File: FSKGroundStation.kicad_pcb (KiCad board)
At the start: 4 copper layers, 100 x 82 mm, 196 parts, among them J1 FTSH-105-01-L-DV-K, J10 CX90B1-24P, J11 HTSW-102-07-G-S, J2 HTSW-102-07-G-S, J22 BWSMA-KWE-Z001, J23 SJ-3524-SMT, J24 HTSW-103-07-G-S, J3 CX90B1-24P, J4 BWSMA-KWE-Z001, J5 BWSMA-KWE-Z001, J9 HTSW-102-07-G-S, Q1 BSS138, Q2 BSS138, U1 TPSM861253RDXR, U10 74LVC1GU04DRL, U2 CC1312R1F3RGZR, U3 CY7C65215-32LTXI, U4 CC1125RHBR, U5 GRF5604, U6 SKYA21003, U7 GRF5604, U8 TPD4E004DRYR, U9 SKYA21003, Y1 OW7EL89CENUYO3YLC-40M, Y2 OW7EL89CANUXK7YLC-48M

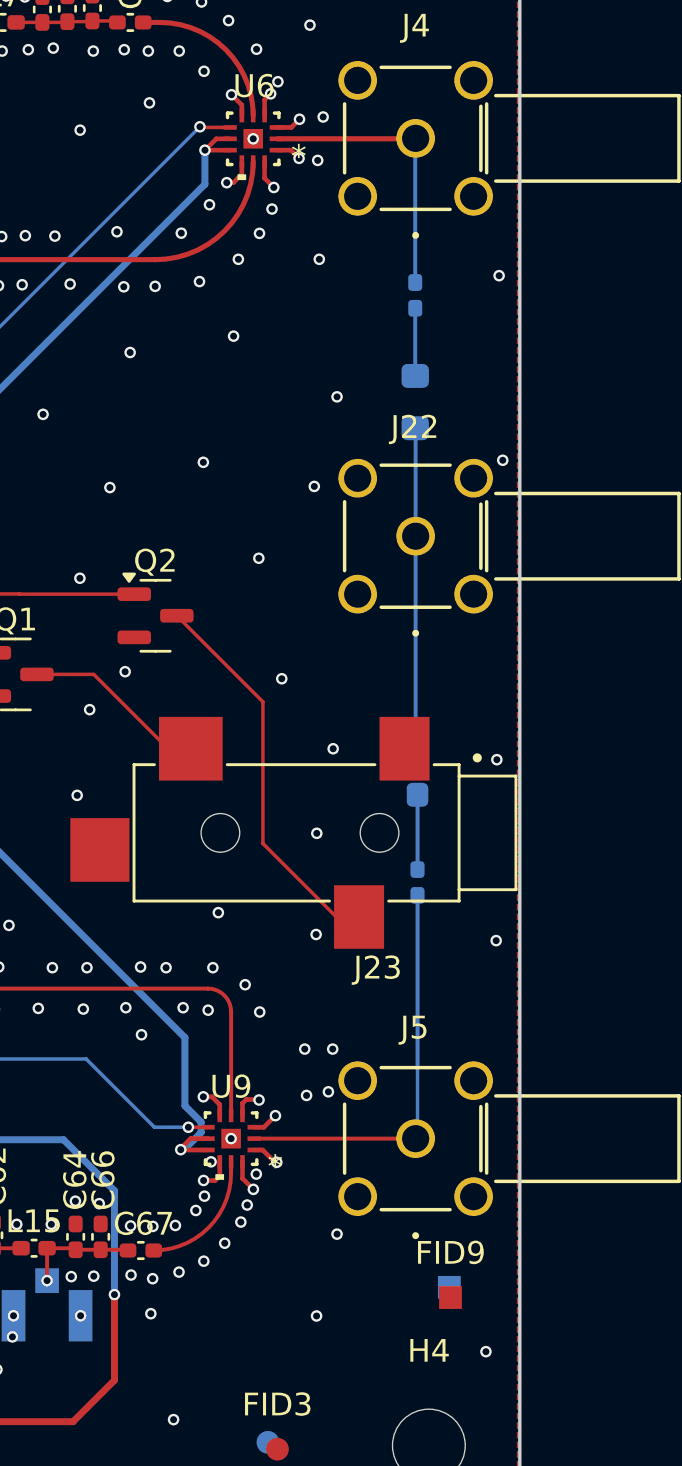
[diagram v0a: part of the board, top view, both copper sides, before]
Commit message: Add bleed-off inductor/resistors to the antenna jacks
Signed-off-by: Corey Minyard <corey@minyard.net>
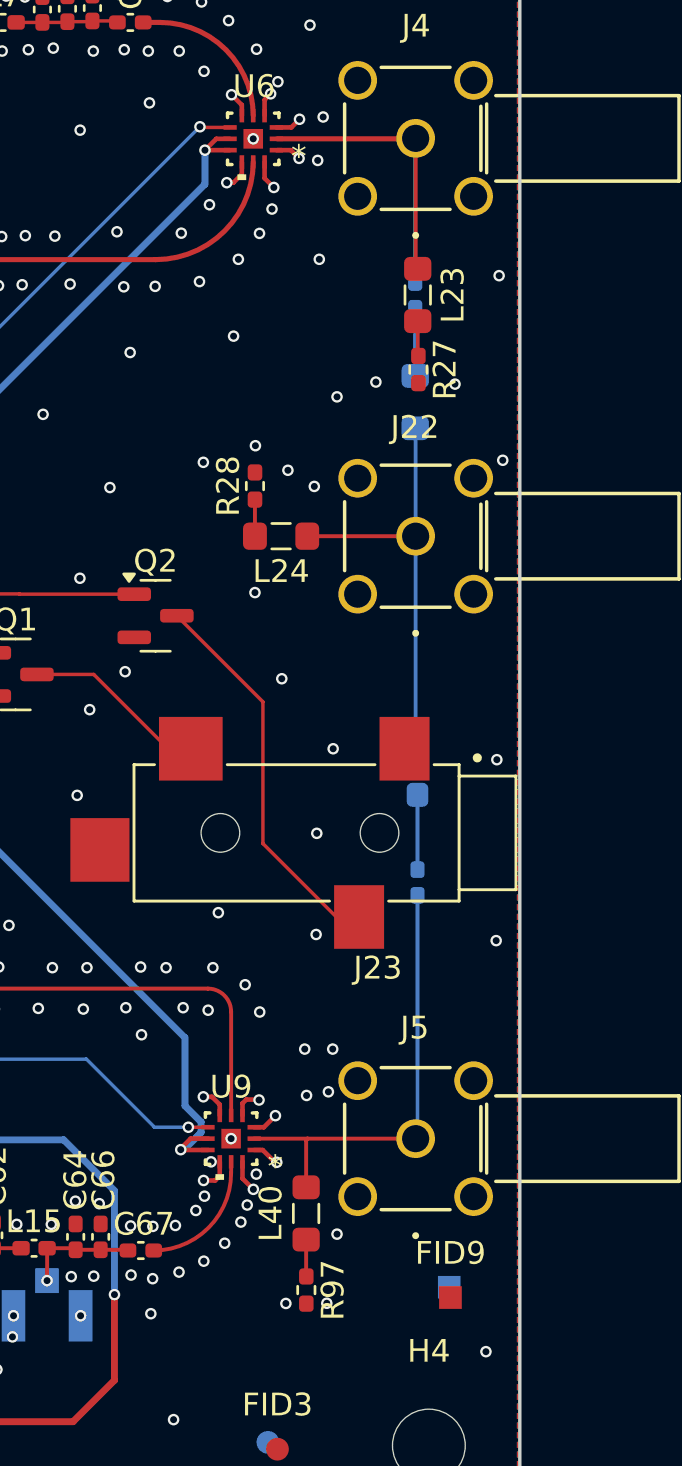
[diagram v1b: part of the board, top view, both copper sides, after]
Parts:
- added L23: 470nH, Inductor_SMD:L_0805_2012Metric_Pad1.05x1.20mm_HandSolder, F.Cu at (165.5, 85.4)
- added L24: 470nH, Inductor_SMD:L_0805_2012Metric_Pad1.05x1.20mm_HandSolder, F.Cu at (159.5, 96.0)
- added L40: 470nH, Inductor_SMD:L_0805_2012Metric_Pad1.05x1.20mm_HandSolder, F.Cu at (160.6, 125.8)
- added R27: 10KΩ, Resistor_SMD:R_0402_1005Metric_Pad0.72x0.64mm_HandSolder, F.Cu at (165.5, 88.7)
- added R28: 10KΩ, Resistor_SMD:R_0402_1005Metric_Pad0.72x0.64mm_HandSolder, F.Cu at (158.3, 93.8)
- added R97: 10KΩ, Resistor_SMD:R_0402_1005Metric_Pad0.72x0.64mm_HandSolder, F.Cu at (160.6, 129.2)
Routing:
- net RF_144: track 12.4 -> 18.2 mm
- net Net-(J22-Pad1): track 14.3 -> 19.0 mm
- net RF_440: track 17.7 -> 19.9 mm
- net Net-(L40-Pad2): track 0.00 -> 1.63 mm
- net Net-(L24-Pad2): track 0.00 -> 1.61 mm
- net Net-(L23-Pad2): track 0.00 -> 1.54 mm
- net GND: vias 605 -> 610

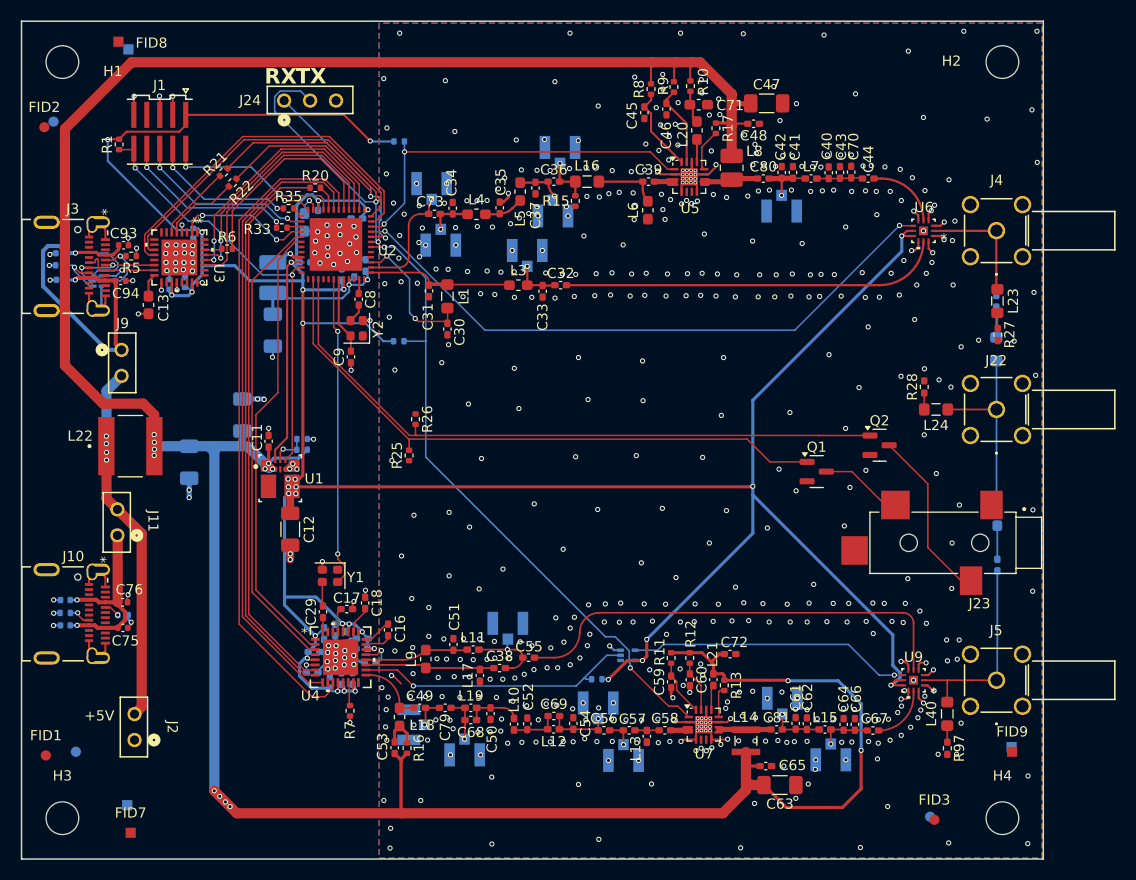
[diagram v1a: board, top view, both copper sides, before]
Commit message: Add a barrel-type power connector
Make supplying power a little simpler.

Signed-off-by: Corey Minyard <corey@minyard.net>
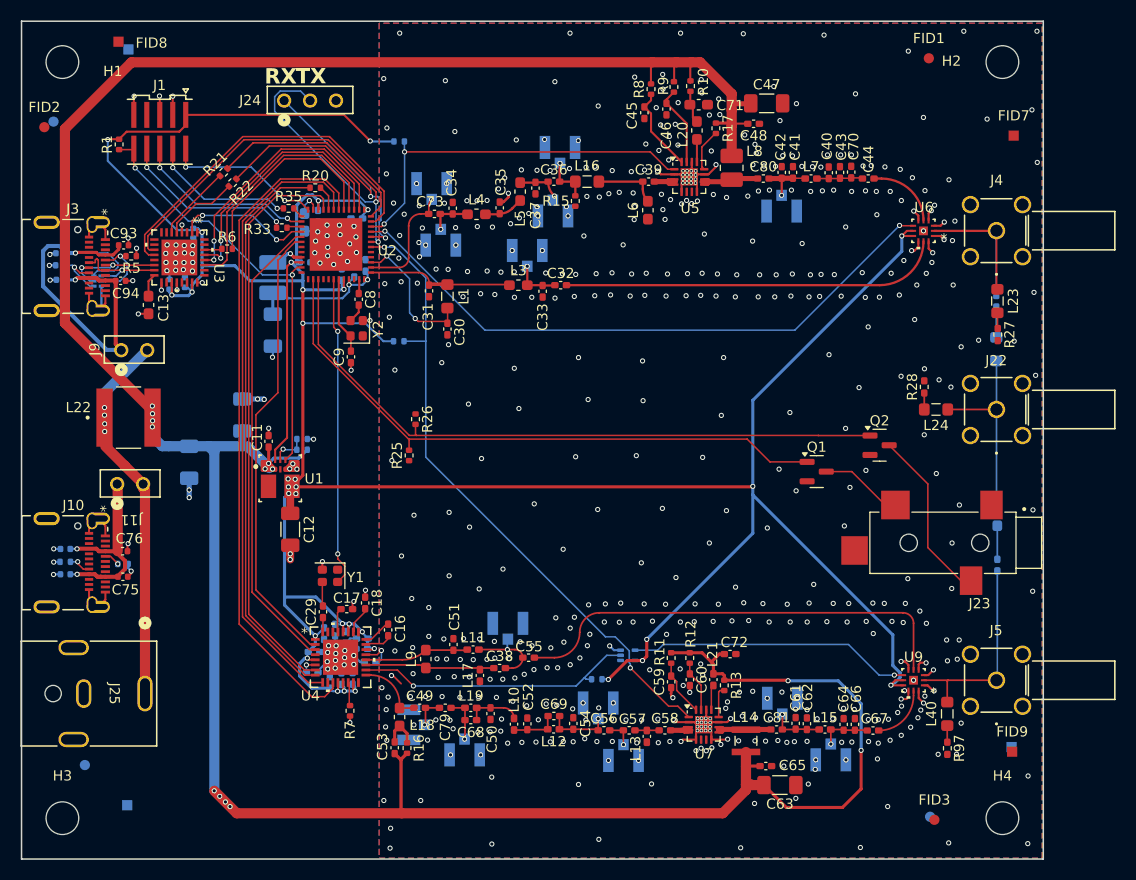
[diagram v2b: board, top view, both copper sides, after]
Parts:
- removed J2: HTSW-102-07-G-S, footprints:CON2_1X2_TU_TSW
- added J25: PJ-063BH, footprints:PJ-063BH_CUD, F.Cu at (82.1, 123.8)
- moved FID1 110.1 mm to (158.8, 61.6)
- moved FID7 110.1 mm to (167.1, 69.2)
- moved C74 5.00 mm to (74.3, 109.7)
- moved C75 5.00 mm to (79.9, 112.4)
- moved C76 5.00 mm to (79.9, 109.9)
- moved C77 5.00 mm to (74.3, 112.1)
- moved J10 5.00 mm to (74.2, 111.0)
- moved R18 5.00 mm to (79.9, 111.1)
- moved R19 5.00 mm to (74.3, 110.9)
- moved J11 3.95 mm to (80.6, 103.3), turned to 0 degrees
- moved L22 2.80 mm to (80.5, 96.8)
- moved J9 1.75 mm to (81.0, 90.2), turned to 0 degrees
- moved FID4 1.57 mm to (76.2, 130.8)
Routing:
- net +5V: track 291.2 -> 288.4 mm
- net Net-(C81-Pad1): track 5.15 -> 6.19 mm
- net +5Vin: track 37.7 -> 38.5 mm
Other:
- board text removed: "+5V"

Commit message: Fix the 440 PA to work at 430-450
Signed-off-by: Corey Minyard <corey@minyard.net>
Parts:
- C66: value 1.8pF 1% -> 5.6pF 1%

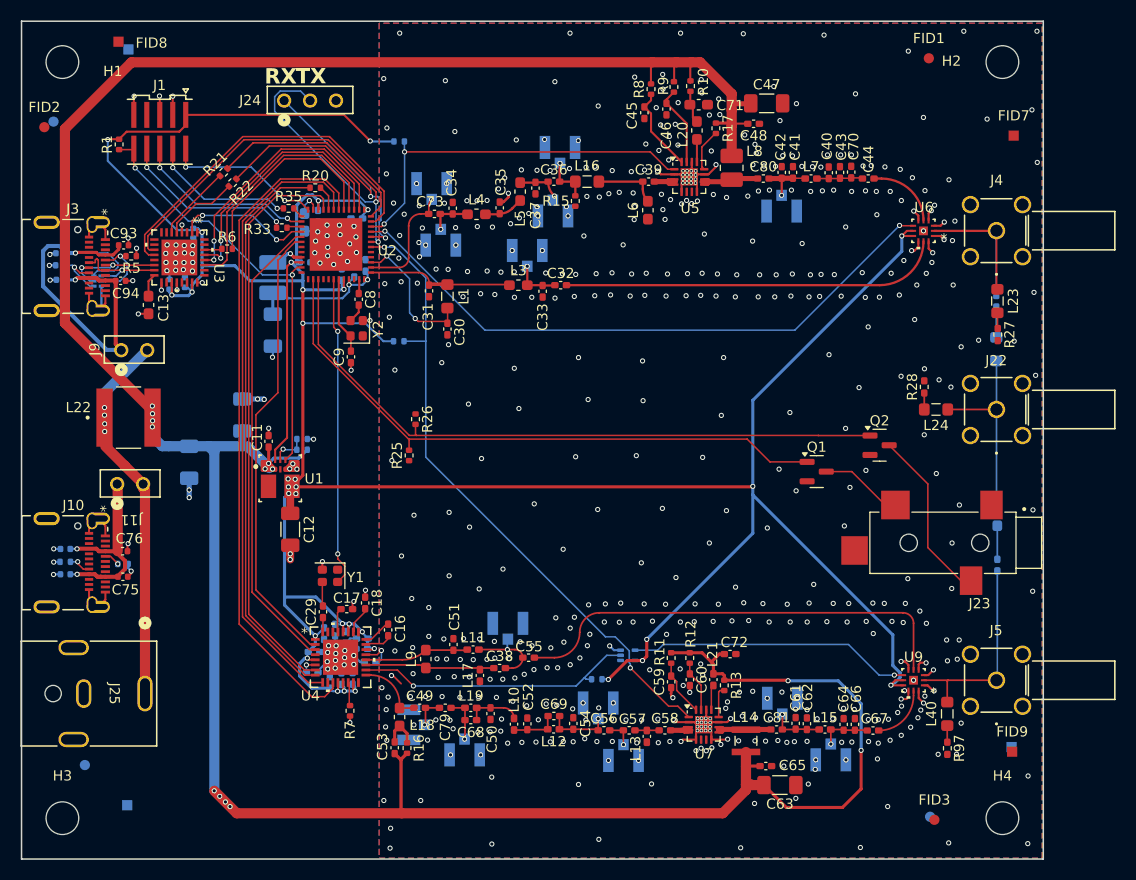
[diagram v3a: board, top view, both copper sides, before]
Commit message: Move RF parts from the bottom of the board to the top
This will allow a heat sink to be more easily mounted.

Signed-off-by: Corey Minyard <corey@minyard.net>
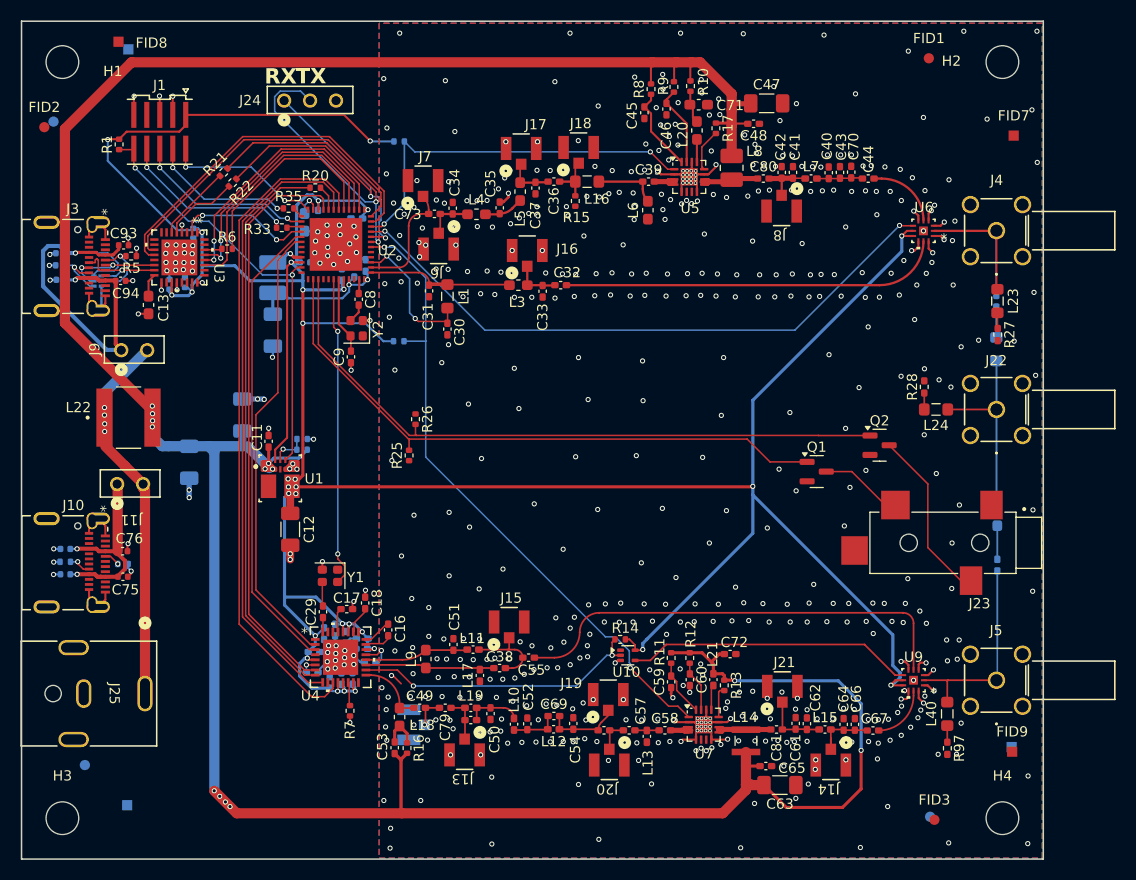
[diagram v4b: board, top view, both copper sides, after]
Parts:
- J13, J14, J15, J16, J17, J18, J19, J20, J21, J6, J7, J8, R14, U10: moved to F.Cu
- moved J17 7.30 mm to (118.9, 70.5)
- moved R14 4.52 mm to (128.6, 118.5)
- moved J18 1.82 mm to (124.5, 70.4), turned to 0 degrees
- moved J20 1.46 mm to (127.5, 130.8), turned to 180 degrees
- moved J19 1.28 mm to (127.4, 123.9), turned to 0 degrees
- moved J21 1.17 mm to (144.5, 123.1), turned to 0 degrees
- moved J7 0.89 mm to (109.3, 73.6), turned to 0 degrees
- moved J14 0.51 mm to (149.2, 130.8), turned to 180 degrees
- moved J6 0.44 mm to (110.8, 80.3), turned to 180 degrees
- moved J15 0.18 mm to (117.7, 116.8), turned to 0 degrees
- turned J13 to 180 degrees
- turned J16 to 0 degrees
- turned J8 to 180 degrees
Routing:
- net +3.3V: track 332.4 -> 328.3 mm, vias 32 -> 30
- net Net-(J21-In): track 5.00 -> 6.20 mm, vias 1 -> 0
- net Net-(J14-In): track 4.88 -> 5.93 mm, vias 1 -> 0
- net 440_TRX_SW: track 27.5 -> 28.5 mm, vias 1 -> 2
- net Net-(J19-In): track 6.08 -> 6.78 mm, vias 1 -> 0
- net GND: track 104.1 -> 103.5 mm, vias 610 -> 609
- net Net-(J20-In): track 2.70 -> 3.20 mm, vias 1 -> 0
- net Net-(U9-CTRL): track 27.7 -> 28.1 mm, vias 1 -> 0
- net Net-(J17-In): track 4.07 -> 4.33 mm, vias 1 -> 0
- net Net-(J6-In): track 3.90 -> 4.13 mm, vias 1 -> 0
- net 144MHz_RF_N: track 11.5 -> 11.8 mm, vias 1 -> 0
- net Net-(J15-In): track 7.93 -> 8.12 mm, vias 1 -> 0
- net Net-(J18-In): track 4.74 -> 4.86 mm, vias 1 -> 0
- net Net-(J8-In): vias 1 -> 0
- net Net-(J16-In): vias 1 -> 0
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
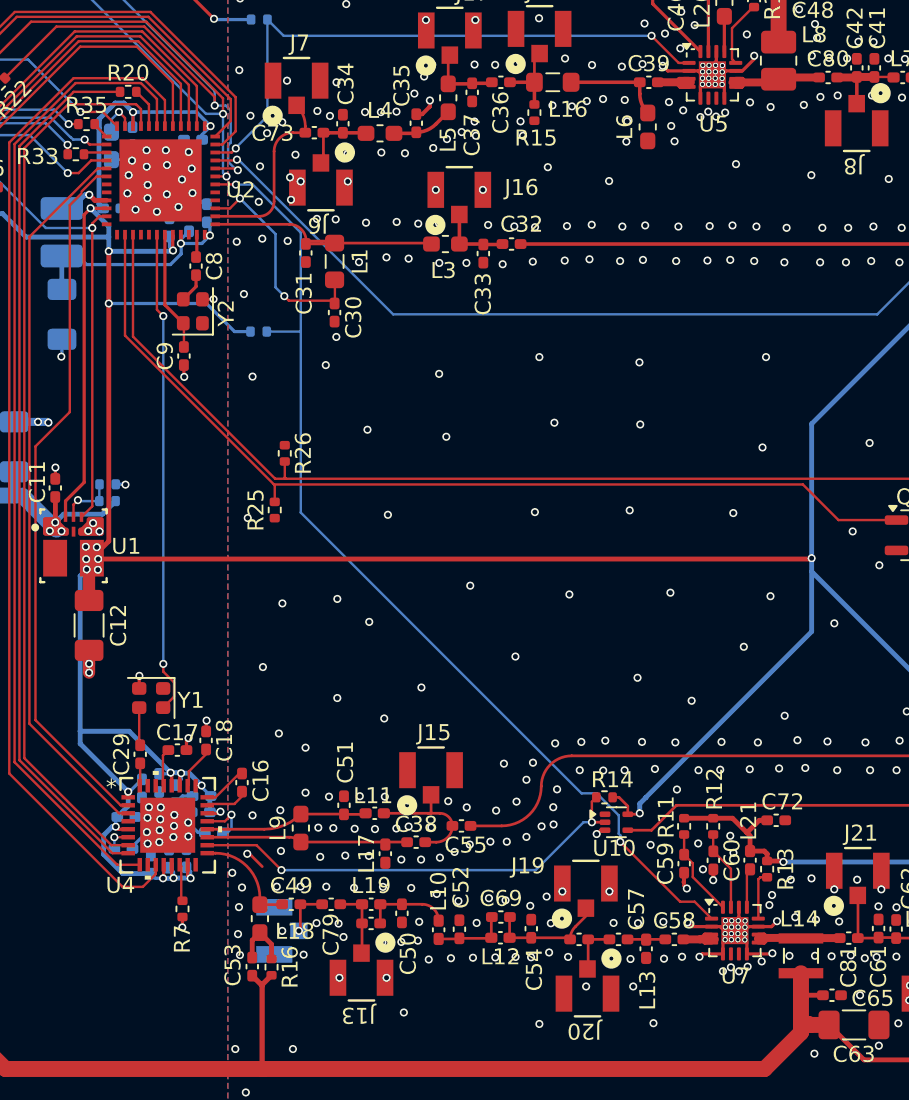
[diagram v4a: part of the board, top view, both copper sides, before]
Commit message: Add thermsistors by the PAs
Signed-off-by: Corey Minyard <corey@minyard.net>
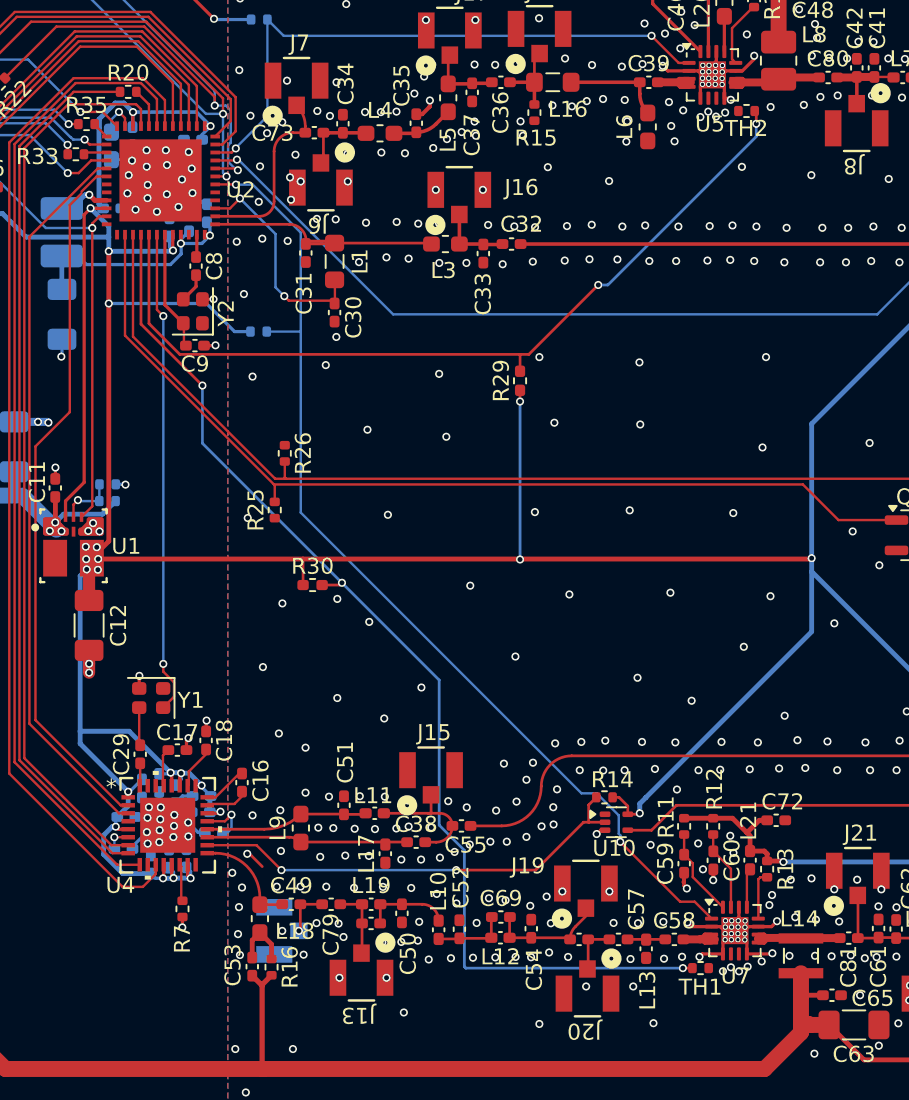
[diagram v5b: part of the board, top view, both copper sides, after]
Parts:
- added R29: 10KΩ 1%, Resistor_SMD:R_0402_1005Metric_Pad0.72x0.64mm_HandSolder, F.Cu at (123.3, 92.4)
- added R30: 10KΩ 1%, Resistor_SMD:R_0402_1005Metric_Pad0.72x0.64mm_HandSolder, F.Cu at (110.3, 105.2)
- added TH1: NTCG103JF103FTDS 10KΩ@25C, Resistor_SMD:R_0402_1005Metric, F.Cu at (134.6, 129.2)
- added TH2: NTCG103JF103FTDS 10KΩ@25C, Resistor_SMD:R_0402_1005Metric, F.Cu at (137.5, 75.5)
- moved C9 0.95 mm to (102.9, 90.2), turned to 180 degrees
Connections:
- U2 pad 40: unconnected-(U2-DIO_27-Pad40) -> 440_PA_TEMP
- U2 pad 41: unconnected-(U2-DIO_28-Pad41) -> 144_PA_TEMP
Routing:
- net 440_PA_TEMP: track 0.00 -> 69.9 mm, vias 0 -> 3
- net 144_PA_TEMP: track 0.00 -> 52.6 mm, vias 0 -> 2
- net +3.3V: track 328.3 -> 340.6 mm, vias 30 -> 32
